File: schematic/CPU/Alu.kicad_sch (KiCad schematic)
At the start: 22 parts, among them U10 74LS245, U101 74LS151, U11 74ABT540, U12 74F521, U2 74LS86, U3 74LS86, U4 74LS86, U5 74LS153, U6 74LS153, U7 74LS153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

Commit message: netlist simulation works
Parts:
- removed unit 2 of U2
- added U104: 74LS04, symbol 74xx:74LS04
- renumbered U4 to U2, U2 to U3, U3 to U4
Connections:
- net flagZ: now also U104.2
- net at U12.19 (P=R): now also U104.1
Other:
- note added: "not instead of xor"
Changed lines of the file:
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@@
   (junction (at 356.87 133.35) (diameter 0) (color 0 0 0 0)
-  )
-  (junction (at 392.43 123.19) (diameter 0) (color 0 0 0 0)
   )
   (junction (at 420.37 200.66) (diameter 0) (color 0 0 0 0)
@@
     (stroke (width 0) (type default) (color 0 0 0 0))
   )
+  (polyline (pts (xy 411.48 128.27) (xy 411.48 111.76))
+    (stroke (width 0) (type default) (color 221 133 0 1))
+  )
   (wire (pts (xy 232.41 146.05) (xy 237.49 146.05))
     (stroke (width 0) (type default) (color 0 0 0 0))
@@
   )
   (wire (pts (xy 323.85 270.51) (xy 323.85 218.44))
-    (stroke (width 0) (type default) (color 0 0 0 0))
-  )
-  (wire (pts (xy 392.43 123.19) (xy 392.43 120.65))
     (stroke (width 0) (type default) (color 0 0 0 0))
   )
@@
     (stroke (width 0) (type default) (color 0 0 0 0))
   )
+  (polyline (pts (xy 391.16 128.27) (xy 411.48 128.27))
+    (stroke (width 0) (type default) (color 221 133 0 1))
+  )
   (wire (pts (xy 101.6 107.95) (xy 105.41 107.95))
     (stroke (width 0) (type default) (color 0 0 0 0))
@@
   )
   (wire (pts (xy 464.82 261.62) (xy 459.74 261.62))
-    (stroke (width 0) (type default) (color 0 0 0 0))
-  )
-  (wire (pts (xy 392.43 125.73) (xy 394.97 125.73))
     (stroke (width 0) (type default) (color 0 0 0 0))
   )
@@
     (stroke (width 0) (type default) (color 0 0 0 0))
   )
-  (wire (pts (xy 392.43 123.19) (xy 392.43 125.73))
-    (stroke (width 0) (type default) (color 0 0 0 0))
-  )
   (wire (pts (xy 105.41 92.71) (xy 128.27 92.71))
     (stroke (width 0) (type default) (color 0 0 0 0))
@@
     (stroke (width 0) (type default) (color 0 0 0 0))
   )
-  (wire (pts (xy 392.43 120.65) (xy 394.97 120.65))
-    (stroke (width 0) (type default) (color 0 0 0 0))
-  )
   (wire (pts (xy 394.97 210.82) (xy 410.21 210.82))
     (stroke (width 0) (type default) (color 0 0 0 0))
@@
     (stroke (width 0) (type default) (color 0 0 0 0))
   )
+  (polyline (pts (xy 391.16 111.76) (xy 391.16 128.27))
+    (stroke (width 0) (type default) (color 221 133 0 1))
+  )
   (wire (pts (xy 237.49 283.21) (xy 237.49 280.67))
     (stroke (width 0) (type default) (color 0 0 0 0))
@@
     (stroke (width 0) (type default) (color 0 0 0 0))
   )
-  (wire (pts (xy 387.35 123.19) (xy 392.43 123.19))
+  (wire (pts (xy 387.35 123.19) (xy 394.97 123.19))
     (stroke (width 0) (type default) (color 0 0 0 0))
   )
@@
     (stroke (width 0) (type default) (color 0 0 0 0))
   )
+  (polyline (pts (xy 391.16 111.76) (xy 411.48 111.76))
+    (stroke (width 0) (type default) (color 221 133 0 1))
+  )
   (wire (pts (xy 464.82 271.78) (xy 459.74 271.78))
     (stroke (width 0) (type default) (color 0 0 0 0))
@@
   (wire (pts (xy 154.94 97.79) (xy 149.86 97.79))
     (stroke (width 0) (type default) (color 0 0 0 0))
+  )
+  (text "not instead of xor" (at 391.16 114.3 0)
+    (effects (font (size 1.27 1.27)) (justify left bottom))
   )
   (label "shift6" (at 151.13 222.25 0)
@@
   (symbol (lib_id "74xx:74LS86") (at 93.98 77.47 0) (unit 1)
     (in_bom yes) (on_board yes)
-    (property "Reference" "U2" (id 0) (at 93.98 69.215 0))
+    (property "Reference" "U3" (id 0) (at 93.98 69.215 0))
     (property "Value" "74LS86" (id 1) (at 93.98 71.5264 0))
     (property "Footprint" "Package_DIP:DIP-14_W7.62mm" (id 2) (at 93.98 77.47 0)
@@
   (symbol (lib_id "74xx:74LS86") (at 95.25 139.7 0) (unit 1)
     (in_bom yes) (on_board yes)
-    (property "Reference" "U3" (id 0) (at 95.25 131.445 0))
+    (property "Reference" "U4" (id 0) (at 95.25 131.445 0))
     (property "Value" "74LS86" (id 1) (at 95.25 133.7564 0))
     (property "Footprint" "Package_DIP:DIP-14_W7.62mm" (id 2) (at 95.25 139.7 0)
@@
   (symbol (lib_id "74xx:74LS86") (at 176.53 184.15 0) (unit 1)
     (in_bom yes) (on_board yes)
-    (property "Reference" "U4" (id 0) (at 176.53 175.895 0))
+    (property "Reference" "U2" (id 0) (at 176.53 175.895 0))
     (property "Value" "74LS86" (id 1) (at 176.53 178.2064 0))
     (property "Footprint" "Package_DIP:DIP-14_W7.62mm" (id 2) (at 176.53 184.15 0)
@@
     (pin "2")
     (pin "3")
-  )
-  (symbol (lib_id "74xx:74LS86") (at 402.59 123.19 0) (unit 2)
-    (in_bom yes) (on_board yes)
-    (property "Reference" "U2" (id 0) (at 402.59 114.935 0))
-    (property "Value" "74LS86" (id 1) (at 402.59 117.2464 0))
-    (property "Footprint" "Package_DIP:DIP-14_W7.62mm" (id 2) (at 402.59 123.19 0)
-      (effects (font (size 1.27 1.27)) hide)
-    )
-    (property "Datasheet" "74xx/74ls86.pdf" (id 3) (at 402.59 123.19 0)
-      (effects (font (size 1.27 1.27)) hide)
-    )
-    (pin "4")
-    (pin "5")
-    (pin "6")
   )
   (symbol (lib_id "74xx:74LS86") (at 81.28 213.36 0) (unit 3)
@@
       (effects (font (size 1.27 1.27)) hide)
     )
+    (pin "1")
+    (pin "2")
+  )
+  (symbol (lib_id "74xx:74LS04") (at 402.59 123.19 0) (unit 1)
+    (in_bom yes) (on_board yes) (fields_autoplaced)
+    (property "Reference" "U104" (id 0) (at 402.59 115.4135 0))
+    (property "Value" "74LS04" (id 1) (at 402.59 118.1886 0))
+    (property "Footprint" "" (id 2) (at 402.59 123.19 0)
+      (effects (font (size 1.27 1.27)) hide)
+    )
+    (property "Datasheet" "http://www.ti.com/lit/gpn/sn74LS04" (id 3) (at 402.59 123.19 0)
+      (effects (font (size 1.27 1.27)) hide)
+    )

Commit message: ttl fpga: factorization works in sim and fpga
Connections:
- no-connect marks 15 -> 16
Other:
- note removed: "not instead of xor"
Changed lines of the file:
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@@
   (no_connect (at 88.9 228.6))
   (no_connect (at 393.7 331.47))
+  (no_connect (at 149.86 114.3))
   (no_connect (at 461.01 323.85))
   (no_connect (at 73.66 231.14))
@@
     (stroke (width 0) (type default) (color 0 0 0 0))
   )
-  (polyline (pts (xy 387.35 130.81) (xy 420.37 130.81))
-    (stroke (width 0) (type default) (color 255 0 0 1))
-  )
   (wire (pts (xy 80.01 90.17) (xy 86.36 90.17))
     (stroke (width 0) (type default) (color 0 0 0 0))
@@
     (stroke (width 0) (type default) (color 0 0 0 0))
   )
-  (polyline (pts (xy 160.02 194.31) (xy 203.2 194.31))
-    (stroke (width 0) (type default) (color 255 0 0 1))
-  )
   (wire (pts (xy 434.34 271.78) (xy 407.67 271.78))
     (stroke (width 0) (type default) (color 0 0 0 0))
@@
     (stroke (width 0) (type default) (color 0 0 0 0))
   )
-  (polyline (pts (xy 387.35 109.22) (xy 387.35 130.81))
-    (stroke (width 0) (type default) (color 255 0 0 1))
-  )
   (wire (pts (xy 151.13 186.69) (xy 168.91 186.69))
     (stroke (width 0) (type default) (color 0 0 0 0))
@@
     (stroke (width 0) (type default) (color 0 0 0 0))
   )
-  (polyline (pts (xy 138.43 247.65) (xy 114.3 247.65))
-    (stroke (width 0) (type default) (color 255 0 0 1))
-  )
   (wire (pts (xy 345.44 158.75) (xy 361.95 158.75))
     (stroke (width 0) (type default) (color 0 0 0 0))
@@
   (wire (pts (xy 480.06 274.32) (xy 469.9 274.32))
     (stroke (width 0) (type default) (color 0 0 0 0))
-  )
-  (polyline (pts (xy 138.43 242.57) (xy 138.43 247.65))
-    (stroke (width 0) (type default) (color 255 0 0 1))
   )
   (wire (pts (xy 151.13 181.61) (xy 162.56 181.61))
@@
     (stroke (width 0) (type default) (color 0 0 0 0))
   )
-  (polyline (pts (xy 370.84 298.45) (xy 487.68 298.45))
-    (stroke (width 0) (type default) (color 255 0 0 1))
-  )
   (wire (pts (xy 410.21 210.82) (xy 434.34 210.82))
     (stroke (width 0) (type default) (color 0 0 0 0))
@@
     (stroke (width 0) (type default) (color 0 0 0 0))
   )
-  (polyline (pts (xy 420.37 109.22) (xy 387.35 109.22))
-    (stroke (width 0) (type default) (color 255 0 0 1))
-  )
   (wire (pts (xy 82.55 146.05) (xy 87.63 146.05))
     (stroke (width 0) (type default) (color 0 0 0 0))
@@
     (stroke (width 0) (type default) (color 0 0 0 0))
   )
-  (polyline (pts (xy 140.97 226.06) (xy 140.97 233.68))
-    (stroke (width 0) (type default) (color 255 0 0 1))
-  )
   (wire (pts (xy 237.49 215.9) (xy 237.49 213.36))
     (stroke (width 0) (type default) (color 0 0 0 0))
@@
     (stroke (width 0) (type default) (color 0 0 0 0))
   )
-  (polyline (pts (xy 165.1 226.06) (xy 140.97 226.06))
-    (stroke (width 0) (type default) (color 255 0 0 1))
-  )
   (wire (pts (xy 394.97 223.52) (xy 394.97 226.06))
     (stroke (width 0) (type default) (color 0 0 0 0))
@@
     (stroke (width 0) (type default) (color 0 0 0 0))
   )
-  (polyline (pts (xy 203.2 194.31) (xy 203.2 166.37))
-    (stroke (width 0) (type default) (color 255 0 0 1))
-  )
   (wire (pts (xy 125.73 245.11) (xy 128.27 245.11))
     (stroke (width 0) (type default) (color 0 0 0 0))
   )
-  (polyline (pts (xy 487.68 298.45) (xy 487.68 367.03))
-    (stroke (width 0) (type default) (color 255 0 0 1))
-  )
   (wire (pts (xy 125.73 241.3) (xy 128.27 241.3))
     (stroke (width 0) (type default) (color 0 0 0 0))
@@
     (stroke (width 0) (type default) (color 0 0 0 0))
   )
-  (polyline (pts (xy 370.84 367.03) (xy 370.84 298.45))
-    (stroke (width 0) (type default) (color 255 0 0 1))
-  )
   (wire (pts (xy 262.89 203.2) (xy 297.18 203.2))
     (stroke (width 0) (type default) (color 0 0 0 0))
@@
     (stroke (width 0) (type default) (color 0 0 0 0))
   )
-  (polyline (pts (xy 160.02 166.37) (xy 160.02 194.31))
-    (stroke (width 0) (type default) (color 255 0 0 1))
-  )
   (wire (pts (xy 394.97 226.06) (xy 394.97 228.6))
     (stroke (width 0) (type default) (color 0 0 0 0))
@@
   (wire (pts (xy 106.68 139.7) (xy 106.68 151.13))
     (stroke (width 0) (type default) (color 0 0 0 0))
-  )
-  (polyline (pts (xy 165.1 233.68) (xy 165.1 226.06))
-    (stroke (width 0) (type default) (color 255 0 0 1))
   )
   (wire (pts (xy 480.06 276.86) (xy 469.9 276.86))
@@
     (stroke (width 0) (type default) (color 0 0 0 0))
   )
-  (polyline (pts (xy 487.68 367.03) (xy 370.84 367.03))
-    (stroke (width 0) (type default) (color 255 0 0 1))
-  )
   (wire (pts (xy 152.4 138.43) (xy 128.27 138.43))
     (stroke (width 0) (type default) (color 0 0 0 0))
@@
     (stroke (width 0) (type default) (color 0 0 0 0))
   )
-  (polyline (pts (xy 203.2 166.37) (xy 160.02 166.37))
-    (stroke (width 0) (type default) (color 255 0 0 1))
-  )
   (wire (pts (xy 367.03 229.87) (xy 367.03 228.6))
     (stroke (width 0) (type default) (color 0 0 0 0))
@@
     (stroke (width 0) (type default) (color 0 0 0 0))
   )
-  (polyline (pts (xy 114.3 242.57) (xy 138.43 242.57))
-    (stroke (width 0) (type default) (color 255 0 0 1))
-  )
   (wire (pts (xy 434.34 276.86) (xy 402.59 276.86))
     (stroke (width 0) (type default) (color 0 0 0 0))
@@
     (stroke (width 0) (type default) (color 0 0 0 0))
   )
-  (polyline (pts (xy 420.37 130.81) (xy 420.37 109.22))
-    (stroke (width 0) (type default) (color 255 0 0 1))
-  )
   (wire (pts (xy 412.75 123.19) (xy 410.21 123.19))
     (stroke (width 0) (type default) (color 0 0 0 0))
@@
     (stroke (width 0) (type default) (color 0 0 0 0))
   )
-  (polyline (pts (xy 114.3 247.65) (xy 114.3 242.57))
-    (stroke (width 0) (type default) (color 255 0 0 1))
-  )
   (wire (pts (xy 102.87 148.59) (xy 105.41 148.59))
     (stroke (width 0) (type default) (color 0 0 0 0))
@@
   (wire (pts (xy 459.74 205.74) (xy 463.55 205.74))
     (stroke (width 0) (type default) (color 0 0 0 0))
-  )
-  (polyline (pts (xy 140.97 233.68) (xy 165.1 233.68))
-    (stroke (width 0) (type default) (color 255 0 0 1))
   )
   (wire (pts (xy 104.14 87.63) (xy 128.27 87.63))
@@
   (wire (pts (xy 154.94 97.79) (xy 149.86 97.79))
     (stroke (width 0) (type default) (color 0 0 0 0))
-  )
-  (text "not instead of xor" (at 391.16 114.3 0)
-    (effects (font (size 1.27 1.27)) (justify left bottom))
   )
   (label "shift6" (at 151.13 222.25 0)
@@
     (pin "1")
   )
-  (symbol (lib_id "power:GND") (at 382.27 234.95 0)
+  (symbol (lib_id "power:GND") (at 382.27 234.95 0) (unit 1)
     (in_bom yes) (on_board yes)
     (property "Reference" "#PWR031" (id 0) (at 382.27 241.3 0)
@@
     (pin "1")
   )
-  (symbol (lib_id "EDiC-rescue:74AS825-74xx") (at 382.27 213.36 0)
+  (symbol (lib_id "EDiC-rescue:74AS825-74xx") (at 382.27 213.36 0) (unit 1)
     (in_bom yes) (on_board yes)
     (property "Reference" "U9" (id 0) (at 382.27 190.9826 0))
@@
     (pin "9")
   )
-  (symbol (lib_id "power:GND") (at 394.97 229.87 0)
+  (symbol (lib_id "power:GND") (at 394.97 229.87 0) (unit 1)
     (in_bom yes) (on_board yes)
     (property "Reference" "#PWR032" (id 0) (at 394.97 236.22 0)
@@
     (pin "1")
   )
-  (symbol (lib_id "power:GND") (at 448.31 347.98 0)
+  (symbol (lib_id "power:GND") (at 448.31 347.98 0) (unit 1)
     (in_bom yes) (on_board yes)
     (property "Reference" "#PWR0313" (id 0) (at 448.31 354.33 0)
@@
     (pin "1")
   )
-  (symbol (lib_id "EDiC-rescue:74AS825-74xx") (at 448.31 326.39 0)
+  (symbol (lib_id "EDiC-rescue:74AS825-74xx") (at 448.31 326.39 0) (unit 1)
     (in_bom yes) (on_board yes)
     (property "Reference" "U97" (id 0) (at 448.31 304.0126 0))
@@
     (pin "9")
   )
-  (symbol (lib_id "power:GND") (at 461.01 342.9 0)
+  (symbol (lib_id "power:GND") (at 461.01 342.9 0) (unit 1)
     (in_bom yes) (on_board yes)
     (property "Reference" "#PWR0314" (id 0) (at 461.01 349.25 0)
@@
     (pin "1")
   )
-  (symbol (lib_id "power:GND") (at 406.4 359.41 0)
+  (symbol (lib_id "power:GND") (at 406.4 359.41 0) (unit 1)
     (in_bom yes) (on_board yes)
     (property "Reference" "#PWR0326" (id 0) (at 406.4 365.76 0)
@@
     (pin "1")
   )
-  (symbol (lib_id "power:+5V") (at 406.4 311.15 0)
+  (symbol (lib_id "power:+5V") (at 406.4 311.15 0) (unit 1)
     (in_bom yes) (on_board yes)
     (property "Reference" "#PWR0325" (id 0) (at 406.4 314.96 0)
@@
     (pin "1")
   )
-  (symbol (lib_id "74xx:74LS151") (at 406.4 334.01 0)
+  (symbol (lib_id "74xx:74LS151") (at 406.4 334.01 0) (unit 1)
     (in_bom yes) (on_board yes)
     (property "Reference" "U101" (id 0) (at 406.4 306.5526 0))
@@
     (pin "9")
   )
-  (symbol (lib_id "power:GND") (at 393.7 351.79 0)
+  (symbol (lib_id "power:GND") (at 393.7 351.79 0) (unit 1)
     (in_bom yes) (on_board yes)
     (property "Reference" "#PWR0324" (id 0) (at 393.7 358.14 0)
@@
     (pin "1")
   )
-  (symbol (lib_id "power:GND") (at 358.14 171.45 0)
+  (symbol (lib_id "power:GND") (at 358.14 171.45 0) (unit 1)
     (in_bom yes) (on_board yes)
     (property "Reference" "#PWR034" (id 0) (at 358.14 177.8 0)
@@
     (pin "2")
   )
-  (symbol (lib_id "Device:R_Network08") (at 485.14 269.24 270)
+  (symbol (lib_id "Device:R_Network08") (at 485.14 269.24 270) (unit 1)
     (in_bom yes) (on_board yes)
     (property "Reference" "RN3" (id 0) (at 486.3084 279.0952 0)
@@
     (pin "9")
   )
-  (symbol (lib_id "power:+5V") (at 492.76 256.54 0)
+  (symbol (lib_id "power:+5V") (at 492.76 256.54 0) (unit 1)
     (in_bom yes) (on_board yes)
     (property "Reference" "#PWR043" (id 0) (at 492.76 260.35 0)

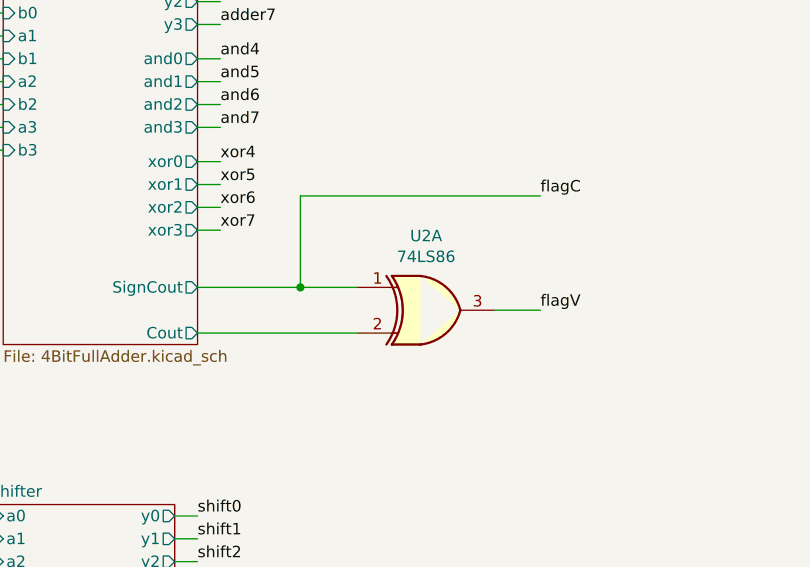
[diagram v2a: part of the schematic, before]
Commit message: carry flag + ram critical path
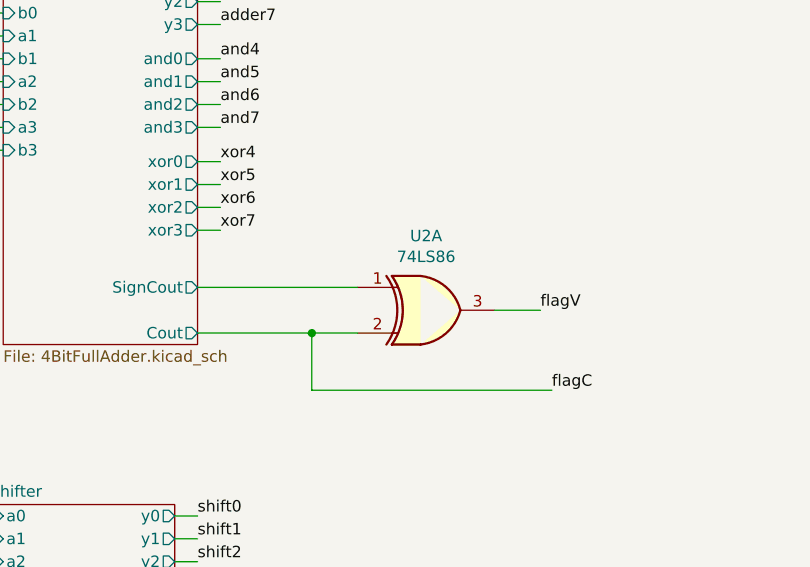
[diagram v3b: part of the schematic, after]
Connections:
- net Adder1/Cout is gone; now on net flagC: U2.2
- net flagC: no longer U2.1
- new net Adder1/SignCout: U2.1
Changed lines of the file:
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@@
   (junction (at 410.21 210.82) (diameter 0) (color 0 0 0 0)
   )
+  (junction (at 163.83 186.69) (diameter 0) (color 0 0 0 0)
+  )
   (junction (at 415.29 205.74) (diameter 0) (color 0 0 0 0)
   )
@@
   )
   (junction (at 417.83 203.2) (diameter 0) (color 0 0 0 0)
-  )
-  (junction (at 162.56 181.61) (diameter 0) (color 0 0 0 0)
   )
   (junction (at 350.52 218.44) (diameter 0) (color 0 0 0 0)
@@
     (stroke (width 0) (type default) (color 0 0 0 0))
   )
-  (wire (pts (xy 151.13 186.69) (xy 168.91 186.69))
+  (wire (pts (xy 151.13 186.69) (xy 163.83 186.69))
     (stroke (width 0) (type default) (color 0 0 0 0))
   )
@@
     (stroke (width 0) (type default) (color 0 0 0 0))
   )
-  (wire (pts (xy 162.56 171.45) (xy 189.23 171.45))
+  (wire (pts (xy 163.83 193.04) (xy 190.5 193.04))
     (stroke (width 0) (type default) (color 0 0 0 0))
   )
@@
     (stroke (width 0) (type default) (color 0 0 0 0))
   )
-  (wire (pts (xy 151.13 181.61) (xy 162.56 181.61))
+  (wire (pts (xy 151.13 181.61) (xy 168.91 181.61))
     (stroke (width 0) (type default) (color 0 0 0 0))
   )
@@
     (stroke (width 0) (type default) (color 0 0 0 0))
   )
+  (wire (pts (xy 163.83 186.69) (xy 168.91 186.69))
+    (stroke (width 0) (type default) (color 0 0 0 0))
+  )
   (wire (pts (xy 299.72 185.42) (xy 262.89 185.42))
     (stroke (width 0) (type default) (color 0 0 0 0))
@@
   )
   (wire (pts (xy 297.18 203.2) (xy 297.18 213.36))
+    (stroke (width 0) (type default) (color 0 0 0 0))
+  )
+  (wire (pts (xy 163.83 186.69) (xy 163.83 193.04))
     (stroke (width 0) (type default) (color 0 0 0 0))
   )
@@
     (stroke (width 0) (type default) (color 0 0 0 0))
   )
-  (wire (pts (xy 162.56 181.61) (xy 168.91 181.61))
-    (stroke (width 0) (type default) (color 0 0 0 0))
-  )
   (wire (pts (xy 480.06 271.78) (xy 469.9 271.78))
     (stroke (width 0) (type default) (color 0 0 0 0))
@@
   )
   (wire (pts (xy 80.01 80.01) (xy 86.36 80.01))
-    (stroke (width 0) (type default) (color 0 0 0 0))
-  )
-  (wire (pts (xy 162.56 181.61) (xy 162.56 171.45))
     (stroke (width 0) (type default) (color 0 0 0 0))
   )
@@
     (effects (font (size 1.27 1.27)) (justify right bottom))
   )
-  (label "flagC" (at 189.23 171.45 0)
+  (label "flagC" (at 190.5 193.04 0)
     (effects (font (size 1.27 1.27)) (justify left bottom))
   )
